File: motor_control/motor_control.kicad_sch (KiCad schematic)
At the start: 6 parts, among them J1 GPIO, U1 CAT24C256

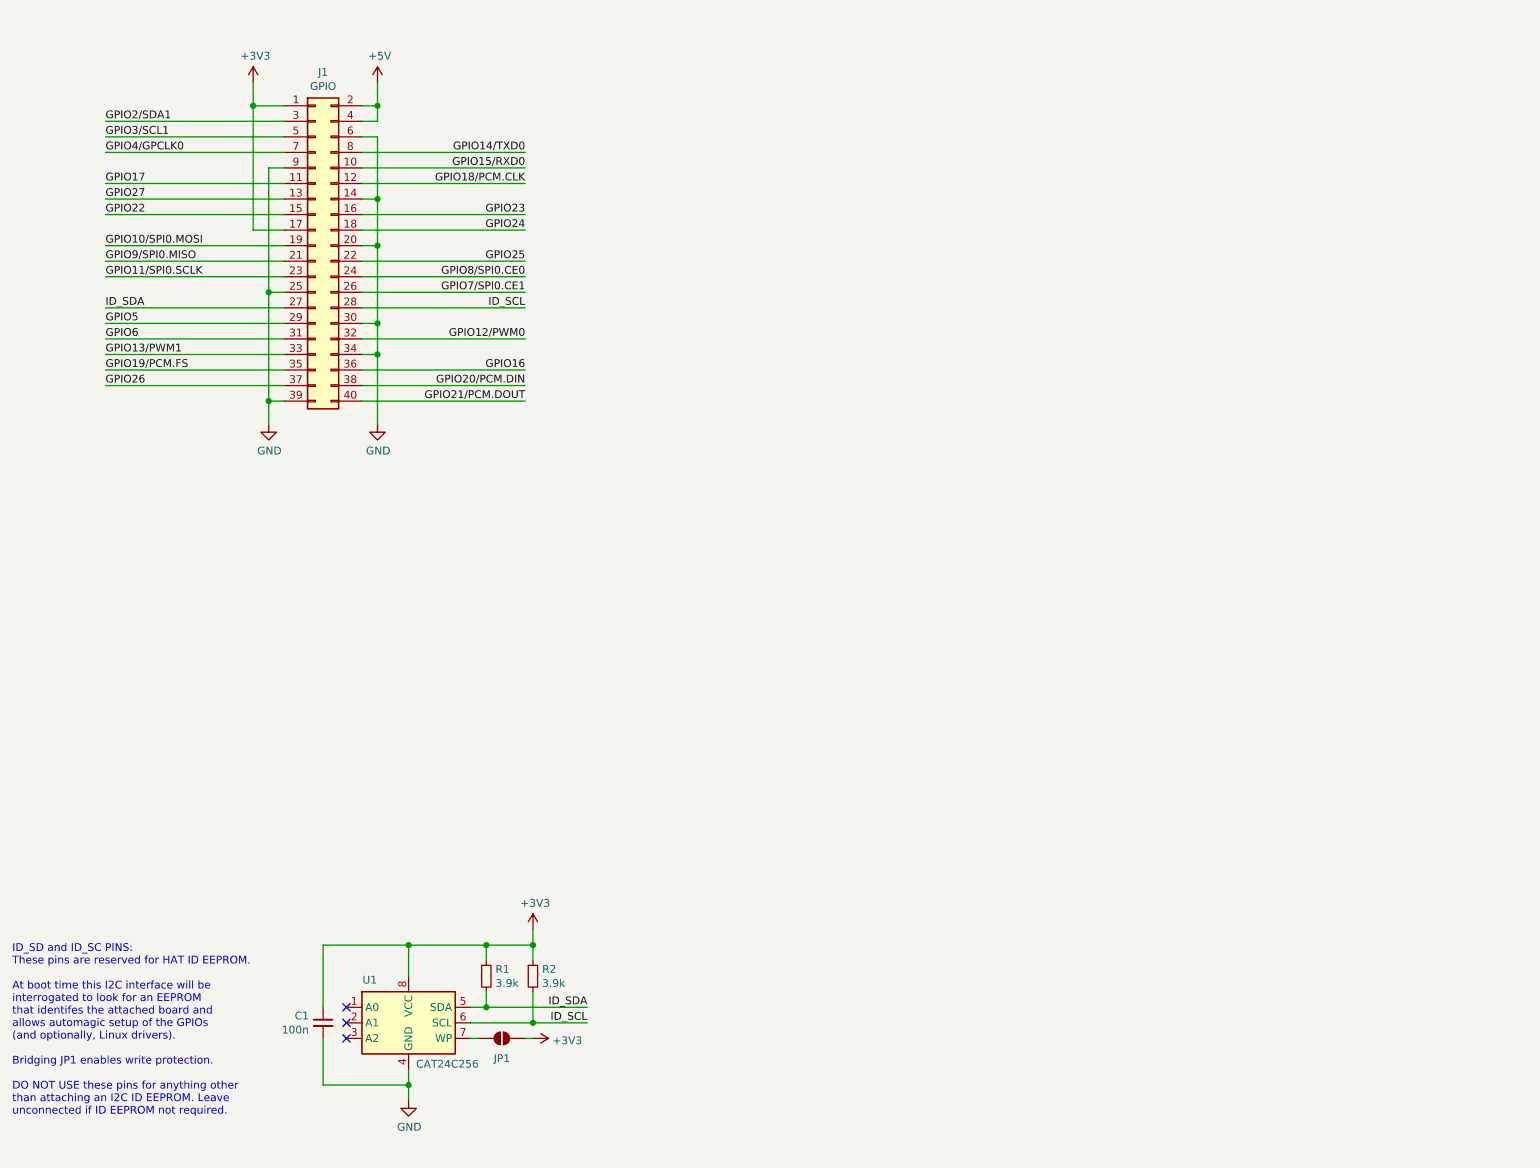
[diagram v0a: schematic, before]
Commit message: add common cathod RGB LED to schematic
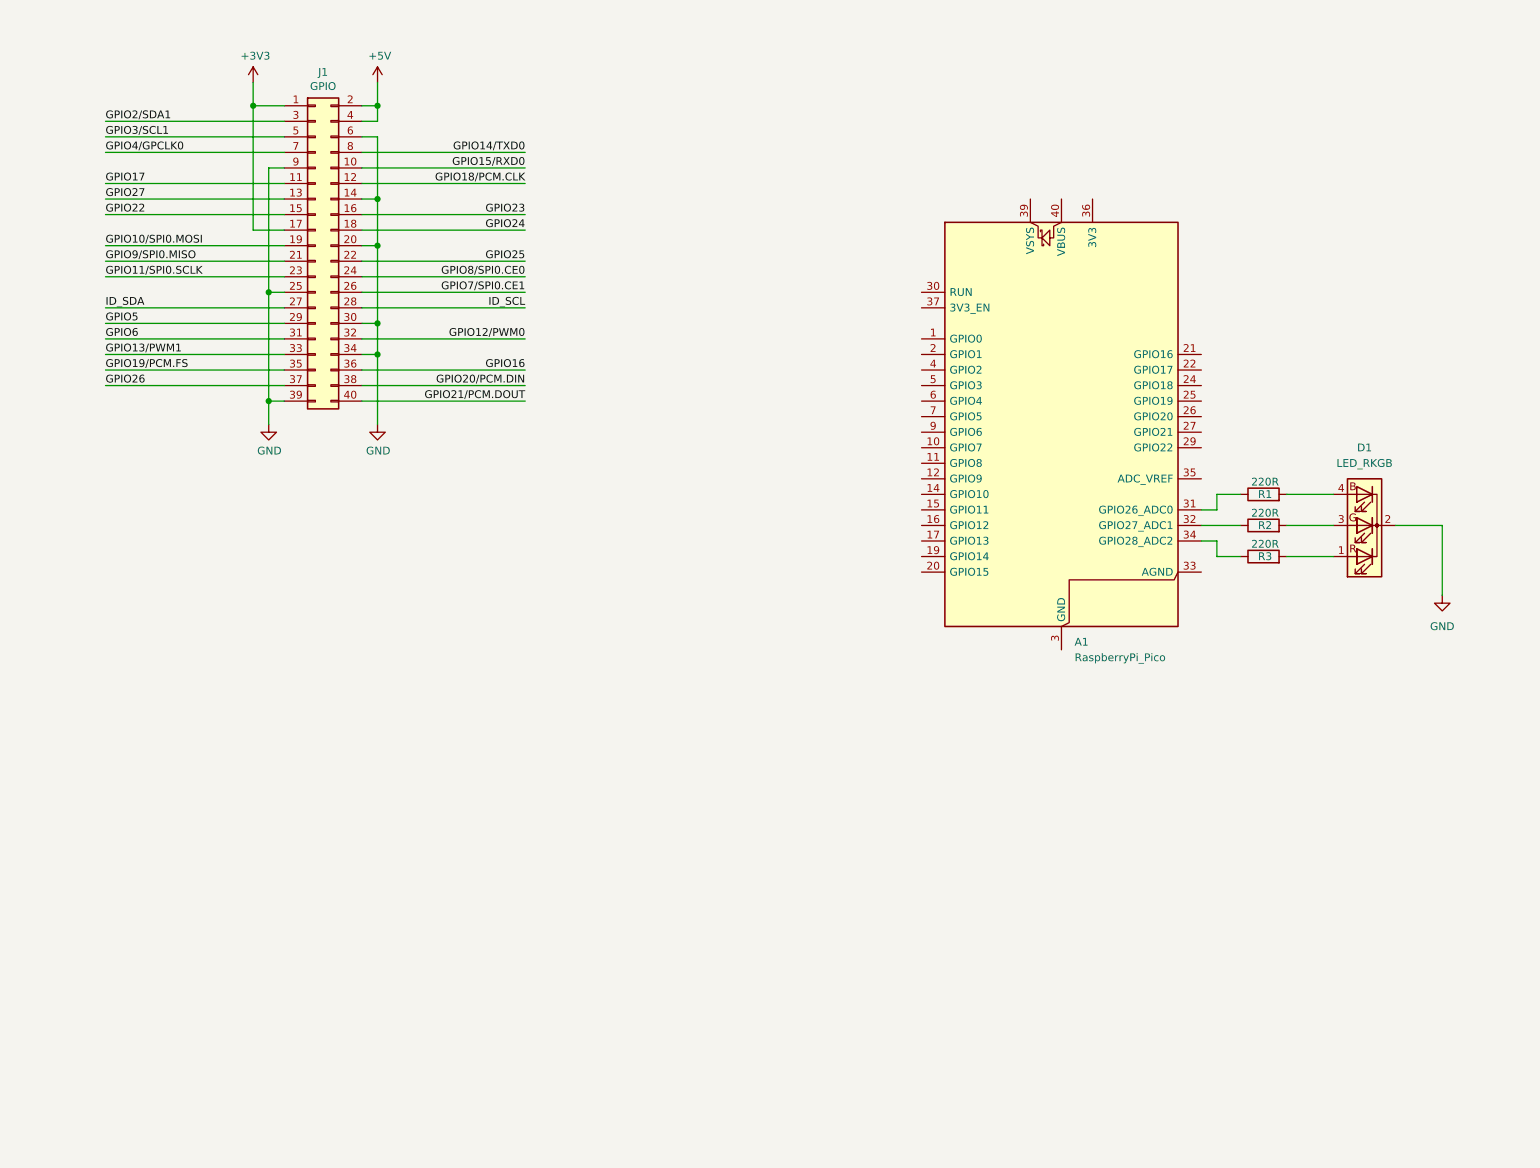
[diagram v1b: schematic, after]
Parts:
- removed C1: 100n, symbol Device:C_Small
- removed JP1: ID_WP, symbol Jumper:SolderJumper_2_Open
- removed R1, R2: 3.9k, symbol Device:R_Small
- removed U1: CAT24C256, symbol Memory_EEPROM:CAT24C256
- added A1: RaspberryPi_Pico, Module:RaspberryPi_Pico_Common_Unspecified, symbol MCU_Module:RaspberryPi_Pico
- added D1: LED_RKGB, symbol Device:LED_RKGB
- added R1, R2, R3: 220R, symbol Device:R
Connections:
- net GND: now also D1.2 (K)
- new net: A1.31 (GPIO26_ADC0), R1.1
- new net: D1.4 (BA), R1.2
- new net: A1.34 (GPIO28_ADC2), R3.1
- new net: D1.1 (RA), R3.2
- new net: D1.3 (GA), R2.2
- new net: A1.13 (GND), A1.18 (GND), A1.23 (GND), A1.28 (GND), A1.3 (GND), A1.38 (GND), A1.8 (GND)
- new net: A1.32 (GPIO27_ADC1), R2.1
- no-connect marks 3 -> 0
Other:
- note removed: "ID_SD and ID_SC PINS: These pins are reserved for HAT ID EEPROM. At boot time this I2C interface will be interrogated to look for an EEPROM that identifes the attached board and allows automagic setup of the GPIOs (and optionally, Linux drivers). Bridging JP1 enables write protection. DO NOT USE these pins for anything other than attaching an I2C ID EEPROM. Leave unconnected if ID EEPROM not requ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"

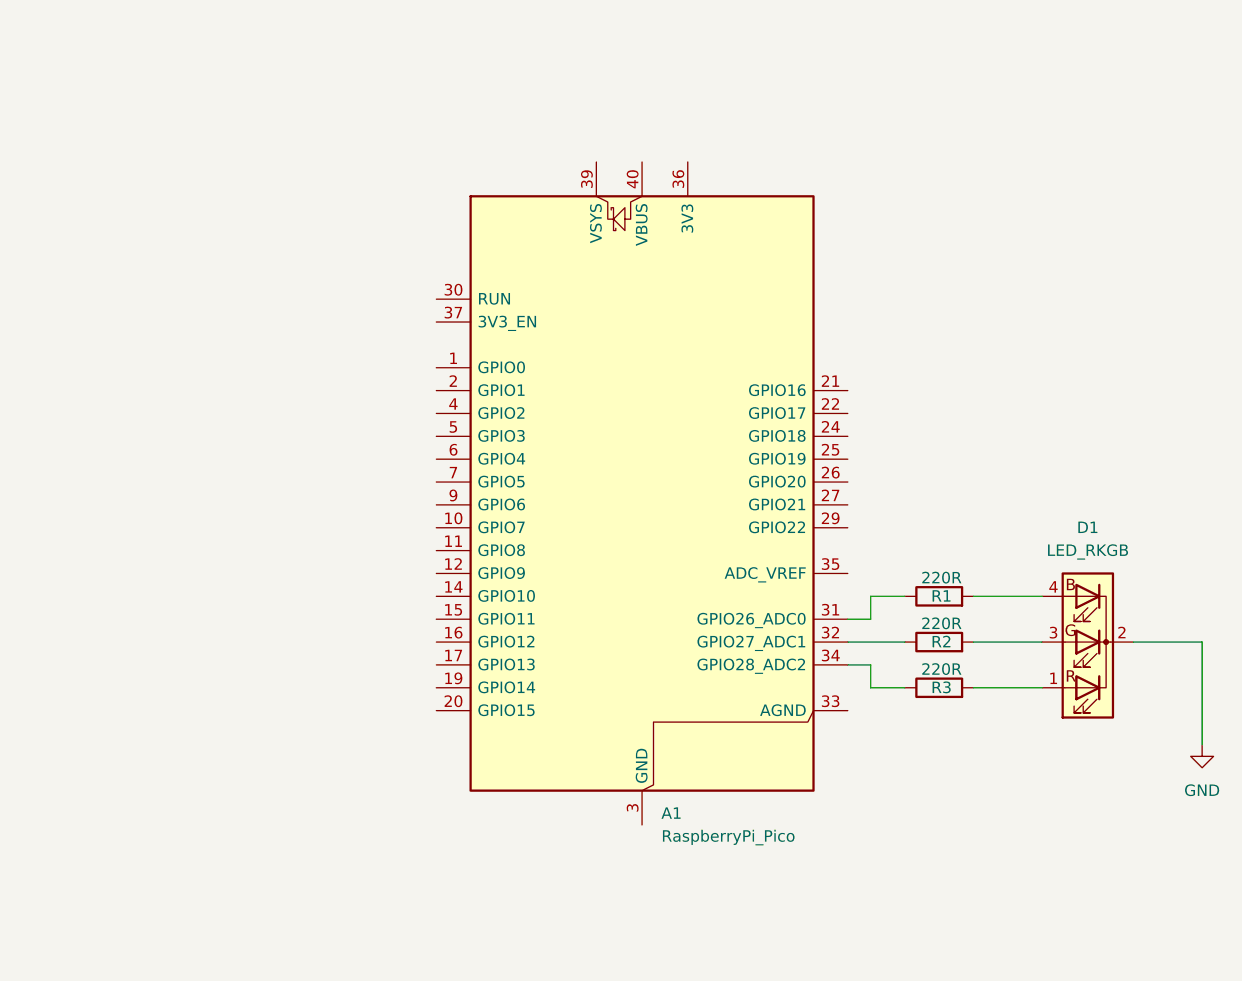
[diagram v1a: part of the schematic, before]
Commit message: add buttons and debounce circuits
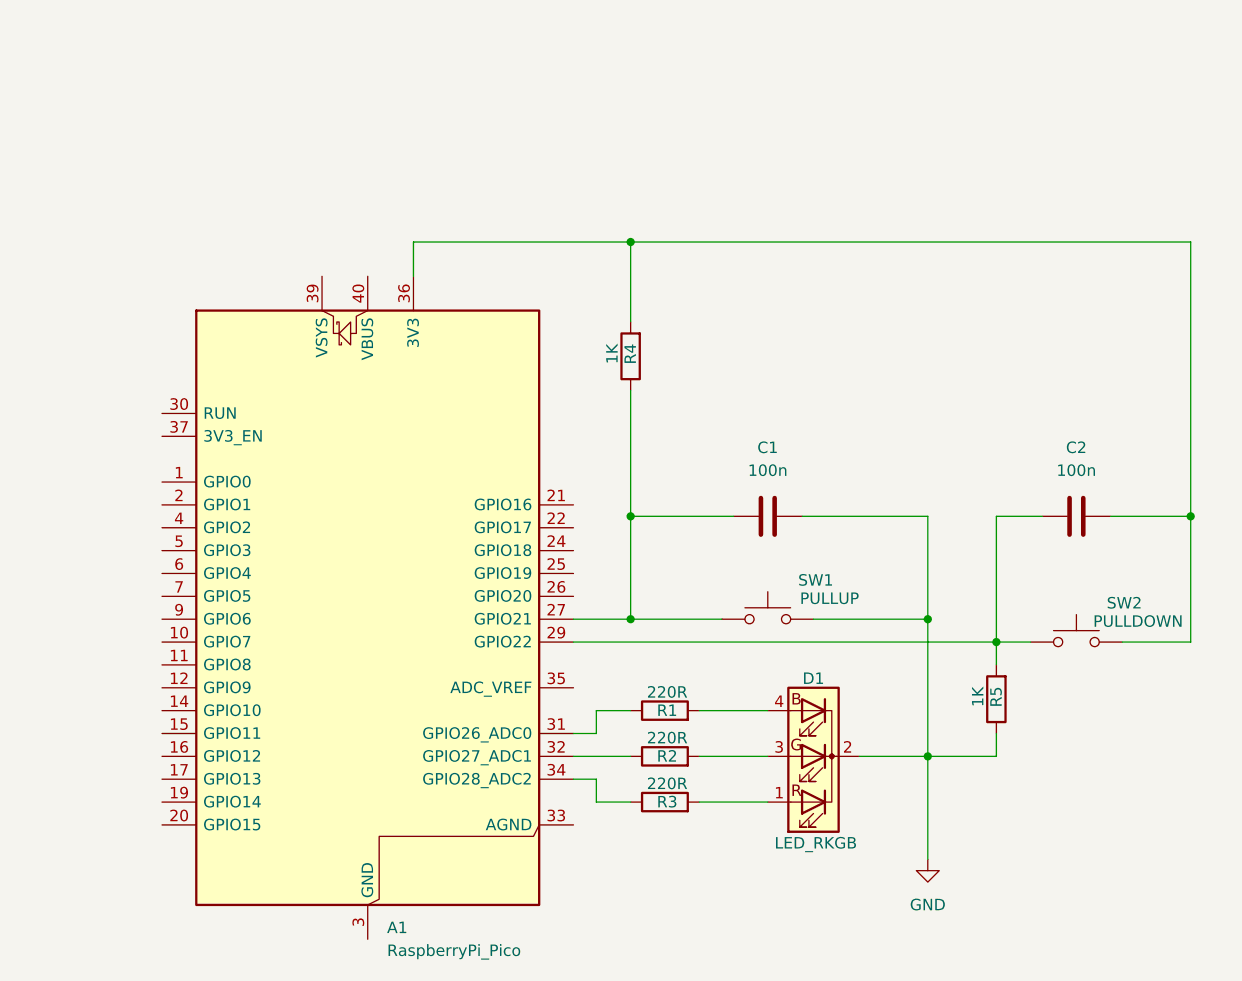
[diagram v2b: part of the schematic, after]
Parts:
- added C1, C2: 100n, symbol Device:C
- added R4, R5: 1K, symbol Device:R
- added SW1: PULLUP, symbol Switch:SW_Push
- added SW2: PULLDOWN, symbol Switch:SW_Push
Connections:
- net GND: now also C1.2, R5.1, SW1.2
- net at A1.27 (GPIO21): now also C1.1, R4.1, SW1.1
- net at A1.29 (GPIO22): now also C2.1, R5.2, SW2.1
- net at A1.36 (3V3): now also C2.2, R4.2, SW2.2
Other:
- moved on the sheet: A1, D1, R1, R2, R3

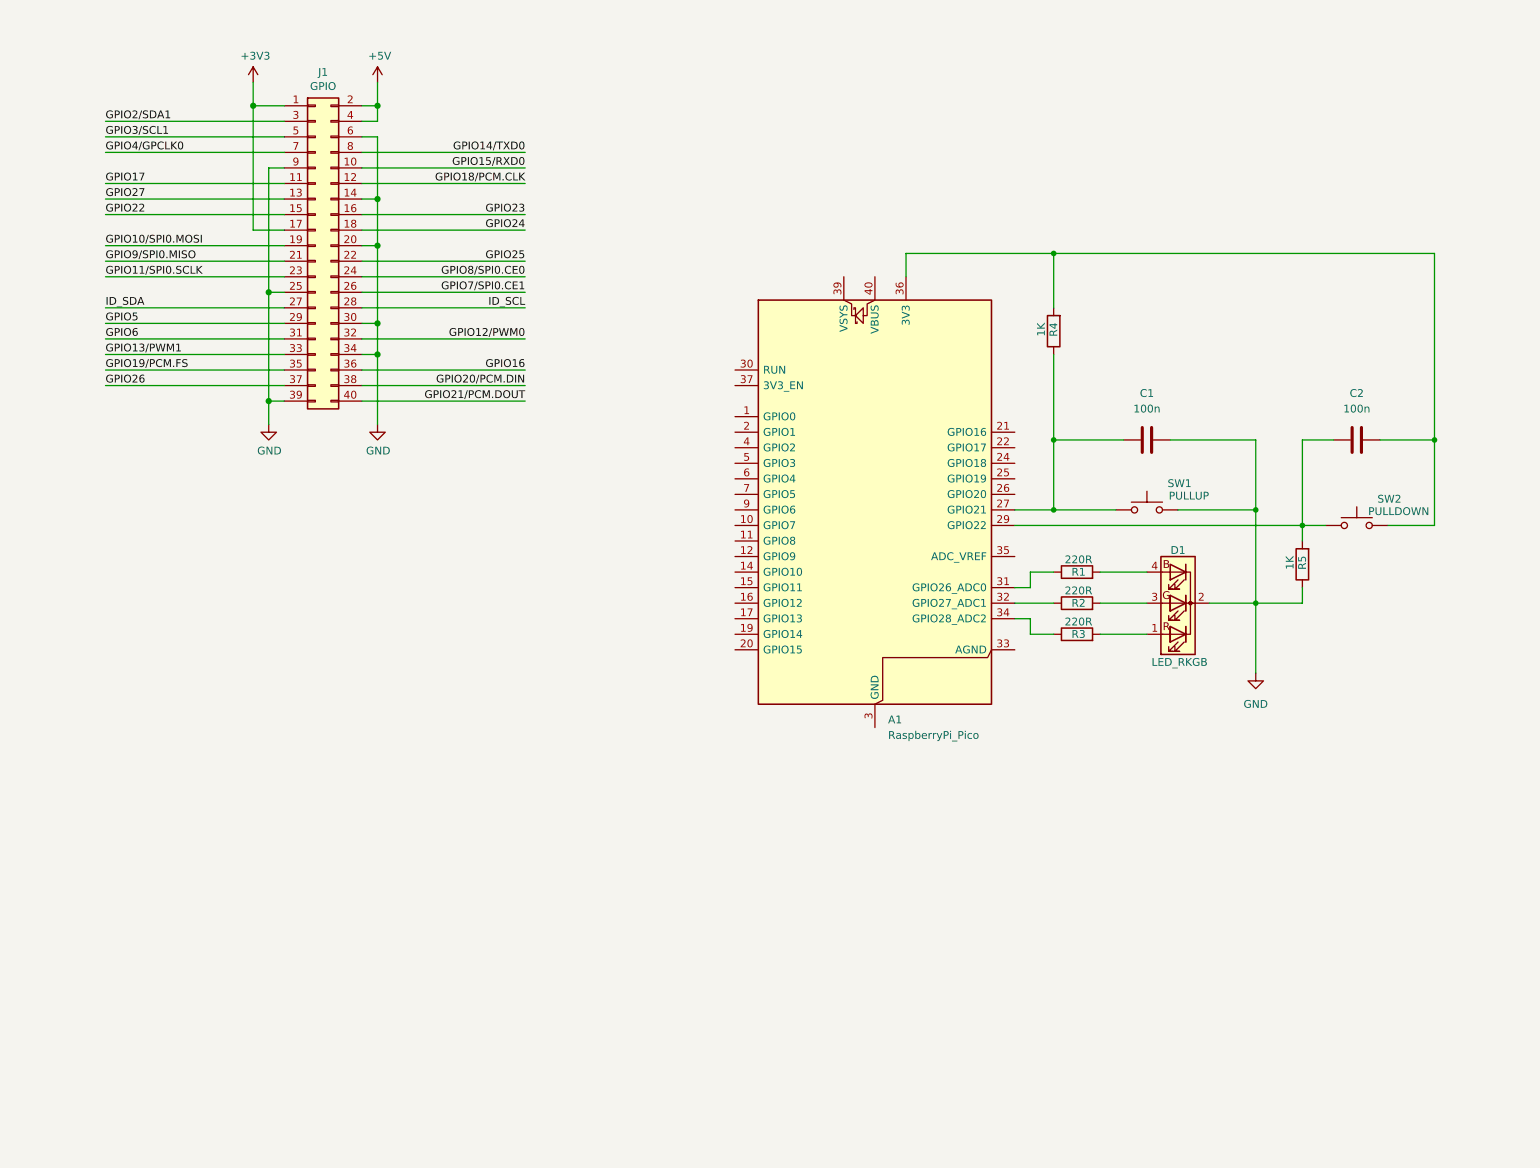
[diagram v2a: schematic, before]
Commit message: use net labels
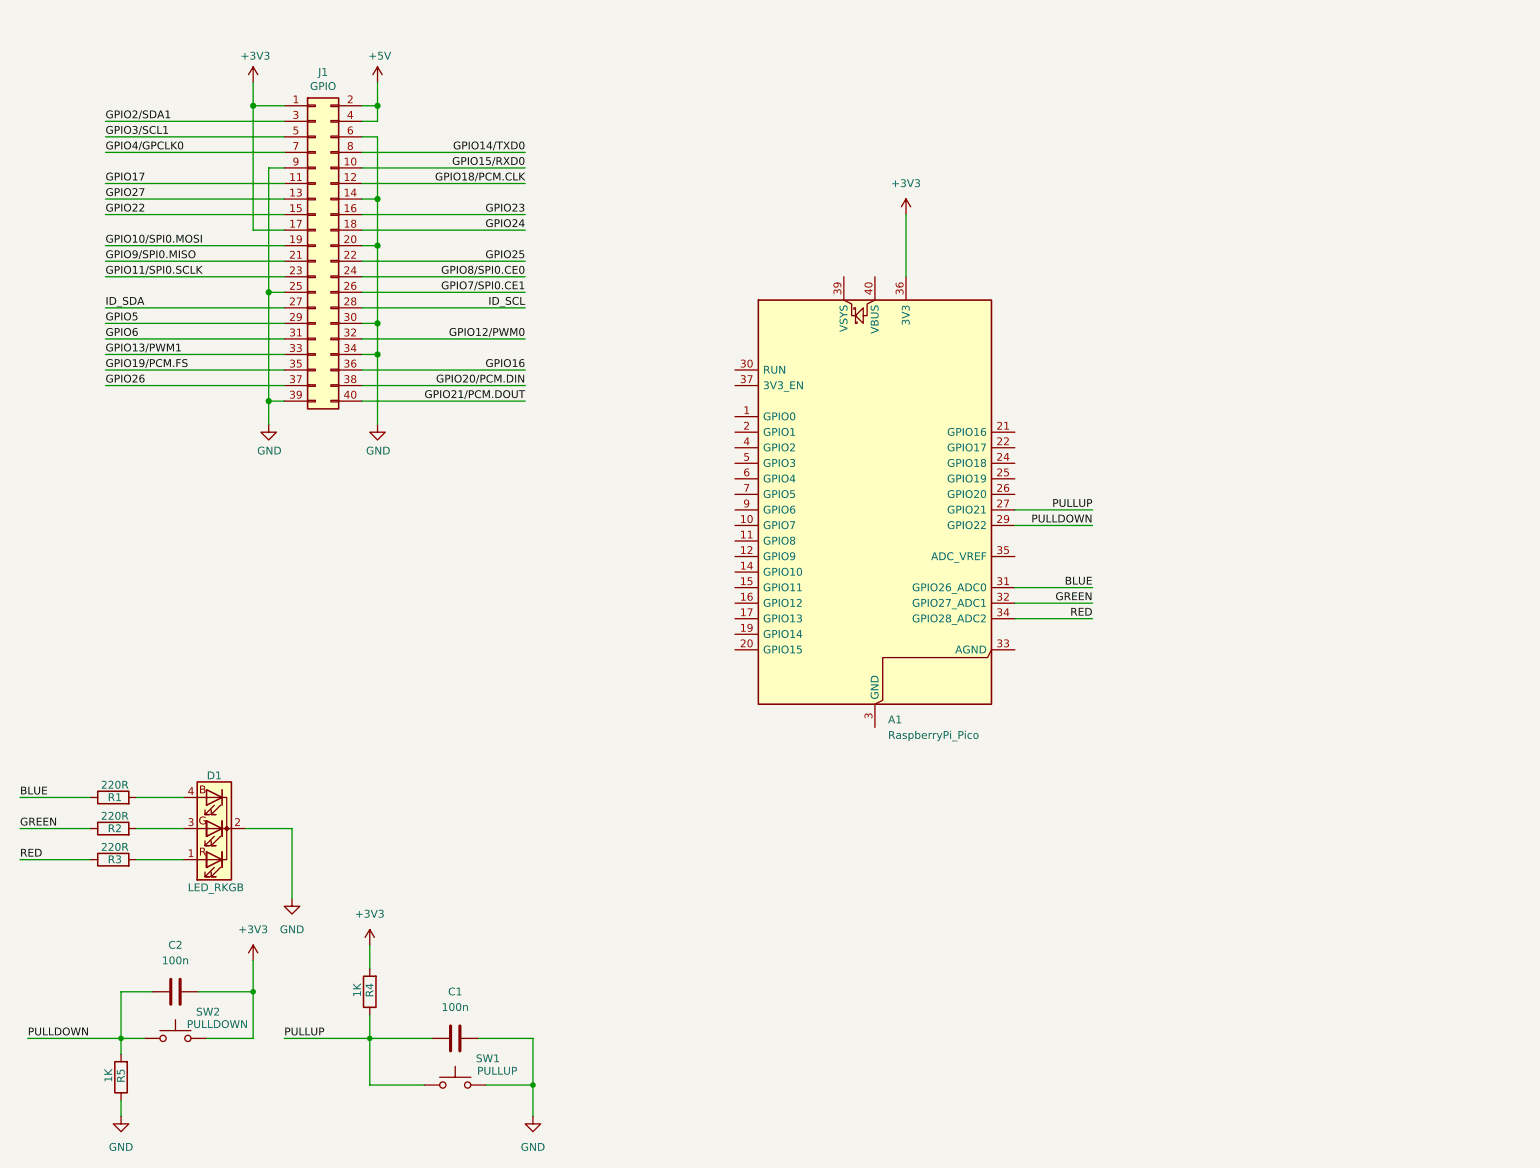
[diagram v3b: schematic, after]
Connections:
- net +3V3: now also A1.36 (3V3), C2.2, R4.2, SW2.2
- net BLUE: now reaches A1.31 (GPIO26_ADC0), R1.1
- net PULLDOWN: now reaches A1.29 (GPIO22), C2.1, R5.2, SW2.1
- net PULLUP: now reaches A1.27 (GPIO21), C1.1, R4.1, SW1.1
- net RED: now reaches A1.34 (GPIO28_ADC2), R3.1
- net GREEN: now reaches A1.32 (GPIO27_ADC1), R2.1
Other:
- moved on the sheet: C1, C2, D1, R1, R2, R3, R4, R5, SW1, SW2
